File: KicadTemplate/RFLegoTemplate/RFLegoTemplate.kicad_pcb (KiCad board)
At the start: 2 copper layers, 32 x 18 mm, 7 parts, among them J1 SMA, J2 SMA

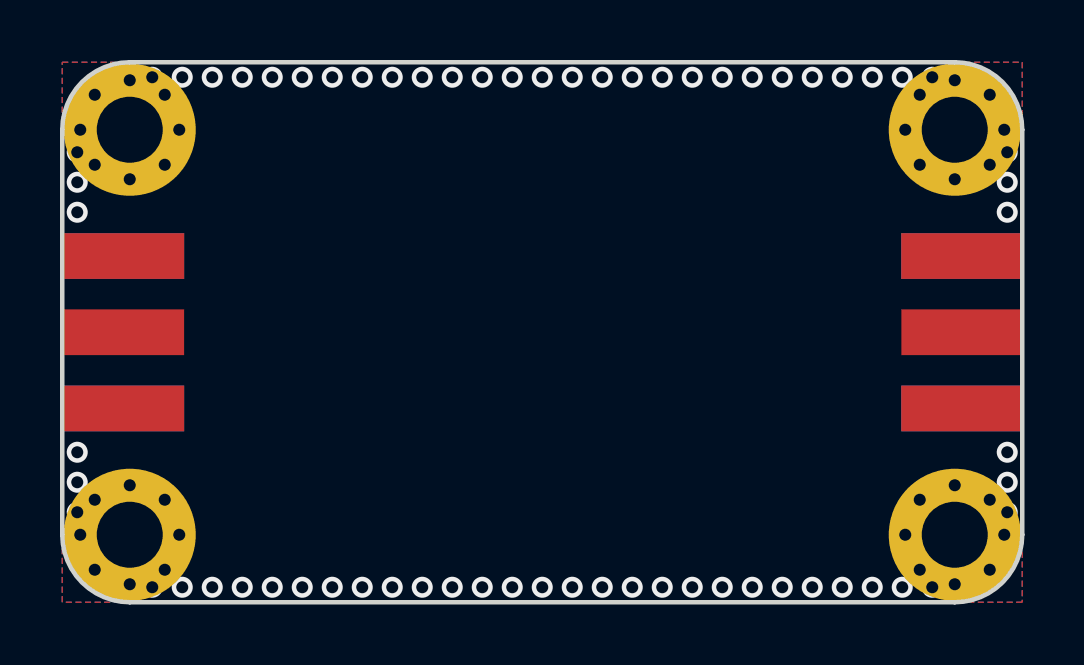
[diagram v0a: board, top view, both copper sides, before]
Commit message: Add SMA connector clearance
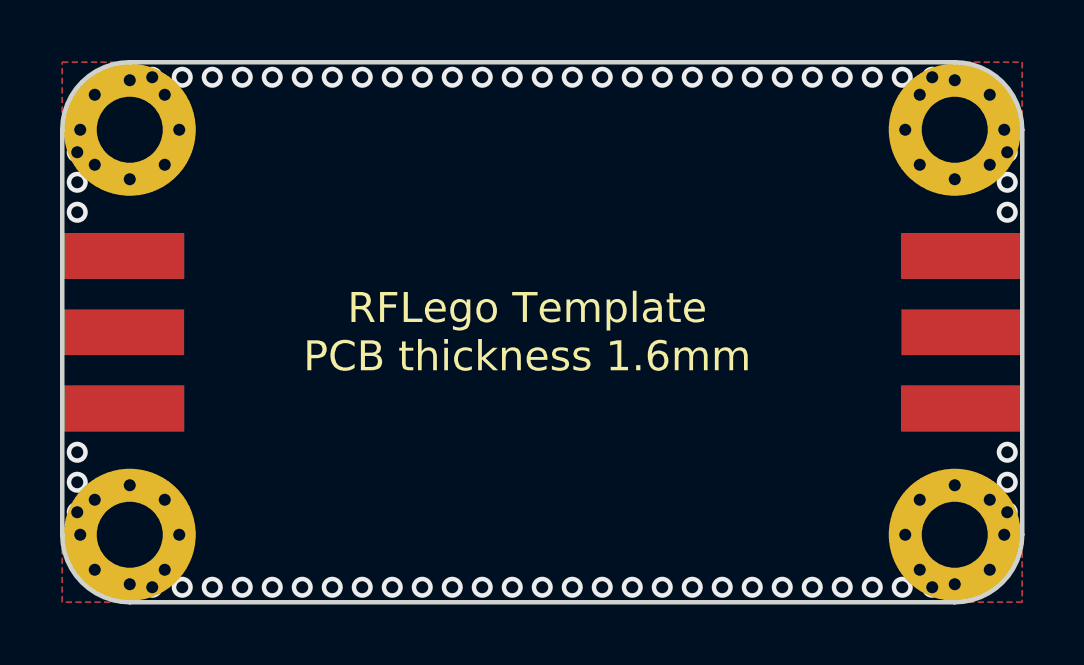
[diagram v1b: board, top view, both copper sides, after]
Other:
- board text added: "RFLego Template PCB thickness 1.6mm"
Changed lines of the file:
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@@
   (general
     (thickness 1.6)
-    (drawings 25)
+    (drawings 36)
     (tracks 66)
     (zones 0)
@@
     (36 B.SilkS user)
     (37 F.SilkS user)
-    (38 B.Mask user hide)
-    (39 F.Mask user hide)
+    (38 B.Mask user)
+    (39 F.Mask user)
     (40 Dwgs.User user)
     (41 Cmts.User user)
@@
       (xy -3.43224 -2.584467) (xy -3.324904 -2.572722) (xy -3.231114 -2.584505)) (layer B.SilkS) (width 0.01))
   )
+  (gr_text "RFLego Template\nPCB thickness 1.6mm" (at 115.5 109) (layer F.SilkS)
+    (effects (font (size 1 1) (thickness 0.25)))
+  )
+  (dimension 18 (width 0.3) (layer Cmts.User)
+    (gr_text "18.000 mm" (at 139.85 109 270) (layer Cmts.User)
+      (effects (font (size 1.5 1.5) (thickness 0.3)))
+    )
+    (feature1 (pts (xy 129.75 118) (xy 138.336421 118)))
+    (feature2 (pts (xy 129.75 100) (xy 138.336421 100)))
+    (crossbar (pts (xy 137.75 100) (xy 137.75 118)))
+    (arrow1a (pts (xy 137.75 118) (xy 137.163579 116.873496)))
+    (arrow1b (pts (xy 137.75 118) (xy 138.336421 116.873496)))
+    (arrow2a (pts (xy 137.75 100) (xy 137.163579 101.126504)))
+    (arrow2b (pts (xy 137.75 100) (xy 138.336421 101.126504)))
+  )
+  (dimension 32 (width 0.3) (layer Cmts.User)
+    (gr_text "32.000 mm" (at 116 124.6) (layer Cmts.User)
+      (effects (font (size 1.5 1.5) (thickness 0.3)))
+    )
+    (feature1 (pts (xy 132 115.75) (xy 132 123.086421)))
+    (feature2 (pts (xy 100 115.75) (xy 100 123.086421)))
+    (crossbar (pts (xy 100 122.5) (xy 132 122.5)))
+    (arrow1a (pts (xy 132 122.5) (xy 130.873496 123.086421)))
+    (arrow1b (pts (xy 132 122.5) (xy 130.873496 121.913579)))
+    (arrow2a (pts (xy 100 122.5) (xy 101.126504 123.086421)))
+    (arrow2b (pts (xy 100 122.5) (xy 101.126504 121.913579)))
+  )
+  (dimension 2.25 (width 0.25) (layer Dwgs.User)
+    (gr_text "2.25 mm" (at 93 116.875 90) (layer Dwgs.User)
+      (effects (font (size 1 1) (thickness 0.25)))
+    )
+    (feature1 (pts (xy 102.25 115.75) (xy 93.913579 115.75)))
+    (feature2 (pts (xy 102.25 118) (xy 93.913579 118)))
+    (crossbar (pts (xy 94.5 118) (xy 94.5 115.75)))
+    (arrow1a (pts (xy 94.5 115.75) (xy 95.086421 116.876504)))
+    (arrow1b (pts (xy 94.5 115.75) (xy 93.913579 116.876504)))
+    (arrow2a (pts (xy 94.5 118) (xy 95.086421 116.873496)))
+    (arrow2b (pts (xy 94.5 118) (xy 93.913579 116.873496)))
+  )
+  (dimension 13.5 (width 0.25) (layer Dwgs.User)
+    (gr_text "13.50 mm" (at 93 109 90) (layer Dwgs.User)
+      (effects (font (size 1 1) (thickness 0.25)))
+    )
+    (feature1 (pts (xy 102.25 102.25) (xy 93.913579 102.25)))
+    (feature2 (pts (xy 102.25 115.75) (xy 93.913579 115.75)))
+    (crossbar (pts (xy 94.5 115.75) (xy 94.5 102.25)))
+    (arrow1a (pts (xy 94.5 102.25) (xy 95.086421 103.376504)))
+    (arrow1b (pts (xy 94.5 102.25) (xy 93.913579 103.376504)))
+    (arrow2a (pts (xy 94.5 115.75) (xy 95.086421 114.623496)))
+    (arrow2b (pts (xy 94.5 115.75) (xy 93.913579 114.623496)))
+  )
+  (dimension 2.25 (width 0.25) (layer Dwgs.User)
+    (gr_text "2.25 mm" (at 93 101.125 90) (layer Dwgs.User)
+      (effects (font (size 1 1) (thickness 0.25)))
+    )
+    (feature1 (pts (xy 102.25 100) (xy 93.913579 100)))
+    (feature2 (pts (xy 102.25 102.25) (xy 93.913579 102.25)))
+    (crossbar (pts (xy 94.5 102.25) (xy 94.5 100)))
+    (arrow1a (pts (xy 94.5 100) (xy 95.086421 101.126504)))
+    (arrow1b (pts (xy 94.5 100) (xy 93.913579 101.126504)))
+    (arrow2a (pts (xy 94.5 102.25) (xy 95.086421 101.123496)))
+    (arrow2b (pts (xy 94.5 102.25) (xy 93.913579 101.123496)))
+  )
+  (dimension 27.5 (width 0.25) (layer Dwgs.User)
+    (gr_text "27.500 mm" (at 116 94.5) (layer Dwgs.User)
+      (effects (font (size 1 1) (thickness 0.25)))
+    )
+    (feature1 (pts (xy 102.25 102.25) (xy 102.25 95.413579)))
+    (feature2 (pts (xy 129.75 102.25) (xy 129.75 95.413579)))
+    (crossbar (pts (xy 129.75 96) (xy 102.25 96)))
+    (arrow1a (pts (xy 102.25 96) (xy 103.376504 95.413579)))
+    (arrow1b (pts (xy 102.25 96) (xy 103.376504 96.586421)))
+    (arrow2a (pts (xy 129.75 96) (xy 128.623496 95.413579)))
+    (arrow2b (pts (xy 129.75 96) (xy 128.623496 96.586421)))
+  )
+  (dimension 2.25 (width 0.25) (layer Dwgs.User)
+    (gr_text "2.250 mm" (at 130.875 94.5) (layer Dwgs.User)
+      (effects (font (size 1 1) (thickness 0.25)))
+    )
+    (feature1 (pts (xy 132 102.25) (xy 132 95.413579)))
+    (feature2 (pts (xy 129.75 102.25) (xy 129.75 95.413579)))
+    (crossbar (pts (xy 129.75 96) (xy 132 96)))
+    (arrow1a (pts (xy 132 96) (xy 130.873496 96.586421)))
+    (arrow1b (pts (xy 132 96) (xy 130.873496 95.413579)))
+    (arrow2a (pts (xy 129.75 96) (xy 130.876504 96.586421)))
+    (arrow2b (pts (xy 129.75 96) (xy 130.876504 95.413579)))
+  )
+  (dimension 2.25 (width 0.25) (layer Dwgs.User)
+    (gr_text "2.250 mm" (at 101.125 94.5) (layer Dwgs.User)
+      (effects (font (size 1 1) (thickness 0.25)))
+    )
+    (feature1 (pts (xy 100 102.25) (xy 100 95.413579)))
+    (feature2 (pts (xy 102.25 102.25) (xy 102.25 95.413579)))
+    (crossbar (pts (xy 102.25 96) (xy 100 96)))
+    (arrow1a (pts (xy 100 96) (xy 101.126504 95.413579)))
+    (arrow1b (pts (xy 100 96) (xy 101.126504 96.586421)))
+    (arrow2a (pts (xy 102.25 96) (xy 101.123496 95.413579)))
+    (arrow2b (pts (xy 102.25 96) (xy 101.123496 96.586421)))
+  )
+  (gr_line (start 132 111.73) (end 132 115.75) (layer F.Mask) (width 2))
+  (gr_line (start 100 111.73) (end 100 115.75) (layer F.Mask) (width 2))
   (gr_text "Line\nRevision 1 - 02/2019\ngithub.com/fgaletsee/RFLego" (at 127.75 106.25) (layer B.SilkS)
     (effects (font (size 1 1) (thickness 0.25)) (justify left mirror))
@@
   (gr_line (start 132 102.25) (end 132 115.75) (layer Edge.Cuts) (width 0.15))
   (gr_line (start 100 102.25) (end 100 115.75) (layer B.Mask) (width 2))
-  (gr_line (start 100 102.25) (end 100 115.75) (layer F.Mask) (width 2))
+  (gr_line (start 100 102.25) (end 100 106.27) (layer F.Mask) (width 2))
   (gr_line (start 102.25 118) (end 129.75 118) (layer B.Mask) (width 2))
   (gr_line (start 102.25 118) (end 129.75 118) (layer F.Mask) (width 2))
@@
   (gr_arc (start 102.25 102.25) (end 102.25 100) (angle -90) (layer Edge.Cuts) (width 0.15))
   (gr_arc (start 102.25 115.75) (end 100 115.75) (angle -90) (layer B.Mask) (width 2))
-  (gr_line (start 132 102.25) (end 132 115.75) (layer F.Mask) (width 2))
+  (gr_line (start 132 102.25) (end 132 106.27) (layer F.Mask) (width 2))
   (gr_line (start 102.25 118) (end 129.75 118) (layer Edge.Cuts) (width 0.15))
   (gr_line (start 100 102.25) (end 100 115.75) (layer Edge.Cuts) (width 0.15))
